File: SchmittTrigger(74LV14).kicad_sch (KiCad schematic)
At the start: 5 parts, among them J2 TBP03R2-350-03BE, J3 TBP03R2-350-03BE, J4 TBP03R2-350-03BE, J5 TBP03R2-350-03BE, U2 74LV14

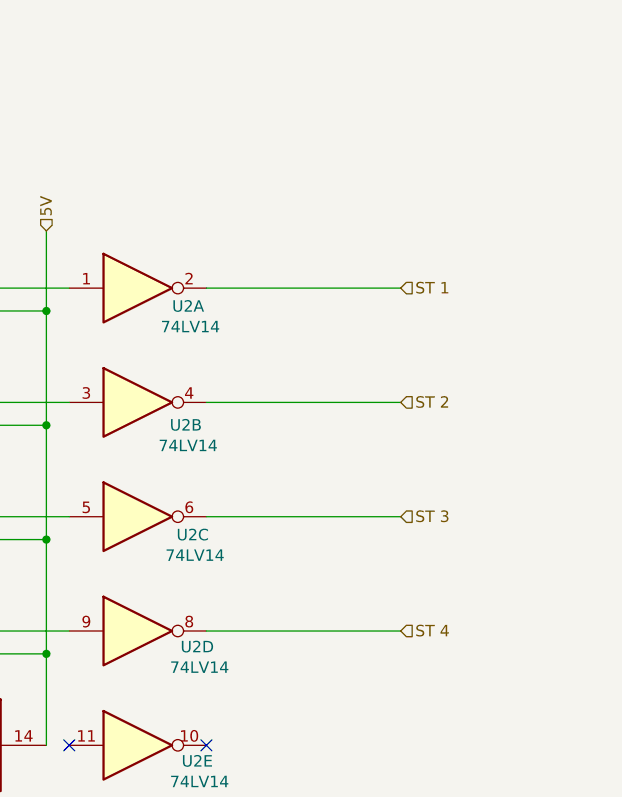
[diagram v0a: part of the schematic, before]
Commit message: Add debug pins and switch
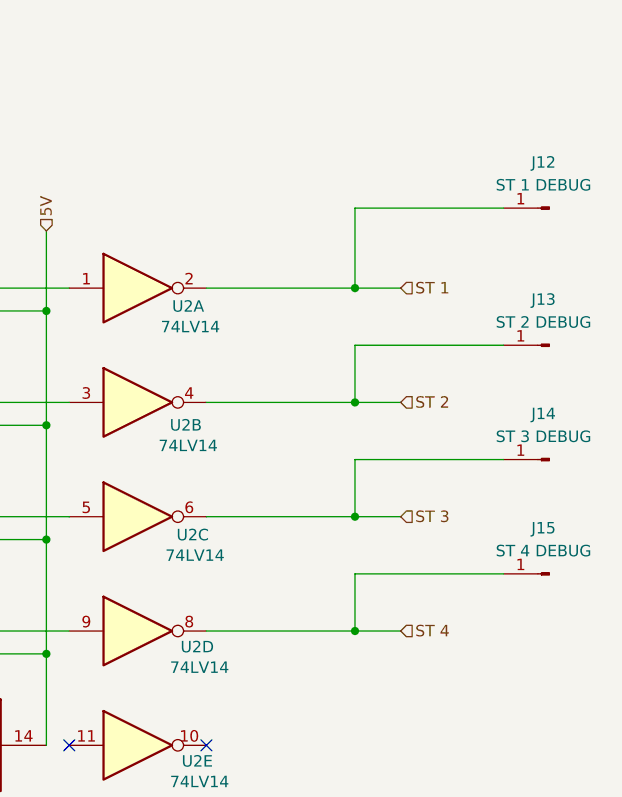
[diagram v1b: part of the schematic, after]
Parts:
- added J12: ST 1 DEBUG, symbol Connector:Conn_01x01_Pin
- added J13: ST 2 DEBUG, symbol Connector:Conn_01x01_Pin
- added J14: ST 3 DEBUG, symbol Connector:Conn_01x01_Pin
- added J15: ST 4 DEBUG, symbol Connector:Conn_01x01_Pin
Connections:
- net ST 1: now also J12.1 (Pin_1)
- net ST 2: now also J13.1 (Pin_1)
- net ST 3: now also J14.1 (Pin_1)
- net ST 4: now also J15.1 (Pin_1)

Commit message: Revert "Add debug pins and switch"
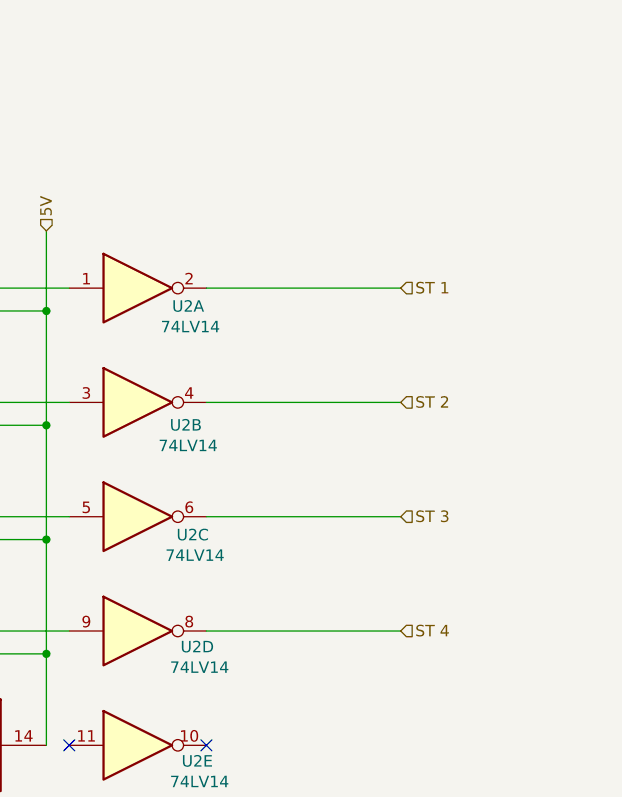
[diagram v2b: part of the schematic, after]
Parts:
- removed J12: ST 1 DEBUG, symbol Connector:Conn_01x01_Pin
- removed J13: ST 2 DEBUG, symbol Connector:Conn_01x01_Pin
- removed J14: ST 3 DEBUG, symbol Connector:Conn_01x01_Pin
- removed J15: ST 4 DEBUG, symbol Connector:Conn_01x01_Pin
